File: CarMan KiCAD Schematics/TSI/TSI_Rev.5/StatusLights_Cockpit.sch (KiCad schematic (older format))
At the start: 18 parts, among them Q3 ZVP1320F, U1 RDE03110S12, U11 TLP293, U13 TLP293

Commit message: Organizational
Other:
- moved on the sheet: D11, Q3, R110, R15, R74, U11
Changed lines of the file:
@@
 $Descr A4 11693 8268
 encoding utf-8
-Sheet 6 6
+Sheet 5 6
 Title ""
 Date ""
@@
 L TSI_Rev.5-rescue:TLP293-CarMan_KiCAD_Library-TSI_Rev.5-rescue U11
 U 1 1 5F9A966C
-P 5900 1650
-F 0 "U11" H 5900 1850 50  0000 C CNN
-F 1 "TLP293" H 5900 1450 50  0000 C CNN
-F 2 "Package_SO:SOIC-4_4.55x2.6mm_P1.27mm" H 5700 1450 50  0001 L CIN
-F 3 "" H 5900 1650 50  0001 L CNN
-	1    5900 1650
+P 10125 3450
+F 0 "U11" H 10125 3650 50  0000 C CNN
+F 1 "TLP293" H 10125 3250 50  0000 C CNN
+F 2 "Package_SO:SOIC-4_4.55x2.6mm_P1.27mm" H 9925 3250 50  0001 L CIN
+F 3 "" H 10125 3450 50  0001 L CNN
+	1    10125 3450
 	1    0    0    -1
 $EndComp
@@
 L Device:R R15
 U 1 1 5F9DEF51
-P 5250 1550
-F 0 "R15" V 5150 1550 50  0000 C CNN
-F 1 "300" V 5250 1550 50  0000 C CNN
-F 2 "Resistor_SMD:R_0805_2012Metric_Pad1.15x1.40mm_HandSolder" V 5180 1550 50  0001 C CNN
-F 3 "~" H 5250 1550 50  0001 C CNN
-	1    5250 1550
+P 9475 3350
+F 0 "R15" V 9375 3350 50  0000 C CNN
+F 1 "300" V 9475 3350 50  0000 C CNN
+F 2 "Resistor_SMD:R_0805_2012Metric_Pad1.15x1.40mm_HandSolder" V 9405 3350 50  0001 C CNN
+F 3 "~" H 9475 3350 50  0001 C CNN
+	1    9475 3350
 	0    1    1    0
 $EndComp
-Text Label 6750 1550 2    50   ~ 0
+Text Label 10975 3350 2    50   ~ 0
 24V
-Text Label 6750 1750 2    50   ~ 0
+Text Label 10975 3550 2    50   ~ 0
 Drive_LED
-Text Label 4400 1750 0    50   ~ 0
-GLV_RTN
-Text Label 4400 1550 0    50   ~ 0
+Text Label 8625 3550 0    50   ~ 0
+GLV_RTN
+Text Label 8625 3350 0    50   ~ 0
 D_LED_CTRL
-Text Label 4700 3200 2    50   ~ 0
+Text Label 4525 3200 2    50   ~ 0
 24V
 Text HLabel 800  5850 0    50   Input ~ 0
@@
 Drive_BTN
 Wire Wire Line
-	5600 1550 5400 1550
+	9825 3350 9625 3350
 Text Notes 7100 6950 0    177  ~ 0
 STATUS LIGHTS, TSAL & RTDS
@@
 	0    1    1    0
 $EndComp
-Connection ~ 4450 3200
-Wire Wire Line
-	4450 3200 5100 3200
-Wire Wire Line
-	3900 3200 4450 3200
+Connection ~ 4275 3200
+Wire Wire Line
+	4275 3200 4925 3200
+Wire Wire Line
+	3725 3200 4275 3200
 $Comp
 L CarMan_KiCAD_Library:D_Schottky D11
 U 1 1 5F9B6857
-P 4450 3600
-F 0 "D11" V 4300 3700 50  0000 C CNN
-F 1 "MMSZ5231B-7-F" H 4450 3726 50  0001 C CNN
-F 2 "Diode_SMD:D_SOD-123" H 4450 3600 50  0001 C CNN
-F 3 "~" H 4450 3600 50  0001 C CNN
-	1    4450 3600
+P 4275 3600
+F 0 "D11" V 4125 3700 50  0000 C CNN
+F 1 "MMSZ5231B-7-F" H 4275 3726 50  0001 C CNN
+F 2 "Diode_SMD:D_SOD-123" H 4275 3600 50  0001 C CNN
+F 3 "~" H 4275 3600 50  0001 C CNN
+	1    4275 3600
 	0    1    1    0
 $EndComp
 Wire Wire Line
-	5100 4725 6150 4725
-Wire Wire Line
-	4450 3900 4800 3900
+	4925 4725 5975 4725
+Wire Wire Line
+	4275 3900 4625 3900
 $Comp
 L Device:Q_PMOS_GSD Q?
 U 1 1 5FC93215
-P 5000 3900
+P 4825 3900
 AR Path="/6196BF15/5FC93215" Ref="Q?"  Part="1"
 AR Path="/5FE1DCBA/5FC93215" Ref="Q3"  Part="1"
-F 0 "Q3" H 5204 3854 50  0000 L CNN
-F 1 "ZVP1320F" H 5204 3945 50  0000 L CNN
-F 2 "TSI_Rev_2021_Footprint_Lib:SOT23" H 5200 4000 50  0001 C CNN
-F 3 "https://www.snapeda.com/parts/ZVP1320FTA/Diodes%20Inc./datasheet/" H 5000 3900 50  0001 C CNN
-	1    5000 3900
+F 0 "Q3" H 5029 3854 50  0000 L CNN
+F 1 "ZVP1320F" H 5029 3945 50  0000 L CNN
+F 2 "TSI_Rev_2021_Footprint_Lib:SOT23" H 5025 4000 50  0001 C CNN
+F 3 "https://www.snapeda.com/parts/ZVP1320FTA/Diodes%20Inc./datasheet/" H 4825 3900 50  0001 C CNN
+	1    4825 3900
 	1    0    0    1
 $EndComp
 Wire Wire Line
-	3050 4100 2850 4100
-Wire Wire Line
 	2250 3900 2050 3900
-Text Notes 5200 4550 0    50   ~ 0
+Text Notes 5025 4550 0    50   ~ 0
 STA20502 RTDS BUZZER (.6A MAX)\n3/1/21 - Pulsed at max of 90mA\n3/1/21 - Tested RTDS, w/Xsistor, worked\n
 Wire Notes Line
-	5100 4575 5100 4625
-Wire Notes Line
-	5050 4375 5150 4375
-Wire Notes Line
-	5050 4575 5050 4375
-Wire Notes Line
-	5150 4575 5050 4575
-Wire Notes Line
-	5150 4375 5150 4575
-Wire Notes Line
-	5100 4325 5100 4375
-Text Label 5550 4725 2    50   ~ 0
-GLV_RTN
-Text Label 6150 4725 2    50   ~ 0
+	4925 4575 4925 4625
+Wire Notes Line
+	4875 4375 4975 4375
+Wire Notes Line
+	4875 4575 4875 4375
+Wire Notes Line
+	4975 4575 4875 4575
+Wire Notes Line
+	4975 4375 4975 4575
+Wire Notes Line
+	4925 4325 4925 4375
+Text Label 5375 4725 2    50   ~ 0
+GLV_RTN
+Text Label 5975 4725 2    50   ~ 0
 RTDS_RTN
-Text Label 5350 4250 0    50   ~ 0
+Text Label 5250 4250 2    50   ~ 0
 RTDS
 Wire Wire Line
-	5100 4250 5350 4250
-Wire Wire Line
-	5100 4100 5100 4250
-Connection ~ 4450 3900
-Wire Wire Line
-	5100 3200 5100 3700
-Text Label 3050 4100 0    50   ~ 0
+	4925 4100 4925 4250
+Connection ~ 4275 3900
+Wire Wire Line
+	4925 3200 4925 3700
+Text Label 3700 4100 2    50   ~ 0
 GLV_RTN
 $Comp
@@
 $EndComp
 Wire Wire Line
-	4450 3450 4450 3200
-Wire Wire Line
-	3900 3450 3900 3200
-Connection ~ 3900 3900
-Wire Wire Line
-	4450 3900 4450 3750
-Wire Wire Line
-	3900 3900 4450 3900
-Wire Wire Line
-	3900 3900 3900 3750
-Wire Wire Line
-	3550 3900 3900 3900
-Wire Wire Line
-	2850 3900 3250 3900
+	4275 3450 4275 3200
+Wire Wire Line
+	3725 3450 3725 3200
+Connection ~ 3725 3900
+Wire Wire Line
+	4275 3900 4275 3750
+Wire Wire Line
+	3725 3900 4275 3900
+Wire Wire Line
+	3725 3900 3725 3750
+Wire Wire Line
+	3375 3900 3725 3900
 $Comp
 L Device:R R74
 U 1 1 5F9BC6E2
-P 3900 3600
-F 0 "R74" H 3970 3646 50  0000 L CNN
-F 1 "40K" V 3900 3550 50  0000 L CNN
-F 2 "Resistor_SMD:R_0805_2012Metric_Pad1.15x1.40mm_HandSolder" V 3830 3600 50  0001 C CNN
-F 3 "~" H 3900 3600 50  0001 C CNN
-	1    3900 3600
+P 3725 3600
+F 0 "R74" H 3795 3646 50  0000 L CNN
+F 1 "40K" V 3725 3550 50  0000 L CNN
+F 2 "Resistor_SMD:R_0805_2012Metric_Pad1.15x1.40mm_HandSolder" V 3655 3600 50  0001 C CNN
+F 3 "~" H 3725 3600 50  0001 C CNN
+	1    3725 3600
 	1    0    0    -1
 $EndComp
@@
 L Device:R R110
 U 1 1 5F9BBE04
-P 3400 3900
-F 0 "R110" V 3300 3900 50  0000 C CNN
-F 1 "10K" V 3400 3900 50  0000 C CNN
-F 2 "Resistor_SMD:R_0805_2012Metric_Pad1.15x1.40mm_HandSolder" V 3330 3900 50  0001 C CNN
-F 3 "~" H 3400 3900 50  0001 C CNN
-	1    3400 3900
+P 3225 3900
+F 0 "R110" V 3125 3900 50  0000 C CNN
+F 1 "10K" V 3225 3900 50  0000 C CNN
+F 2 "Resistor_SMD:R_0805_2012Metric_Pad1.15x1.40mm_HandSolder" V 3155 3900 50  0001 C CNN
+F 3 "~" H 3225 3900 50  0001 C CNN
+	1    3225 3900
 	0    1    1    0
 $EndComp
@@
 	4400 7000 5000 7000
 Wire Wire Line
-	4400 1550 5100 1550
-Wire Wire Line
-	4400 1750 5600 1750
-Wire Wire Line
-	6200 1550 6750 1550
-Wire Wire Line
-	6200 1750 6750 1750
+	8625 3350 9325 3350
+Wire Wire Line
+	8625 3550 9825 3550
+Wire Wire Line
+	10425 3350 10975 3350
+Wire Wire Line
+	10425 3550 10975 3550
 Wire Notes Line
 	500  2100 2250 2100
@@
 GLV_RTN
 Wire Wire Line
-	5100 4250 5100 4325
-Connection ~ 5100 4250
-Wire Wire Line
-	5100 4625 5100 4725
+	4925 4250 4925 4325
+Connection ~ 4925 4250
+Wire Wire Line
+	4925 4625 4925 4725
+Wire Wire Line
+	4925 4250 5250 4250
+Wire Wire Line
+	2850 3900 3075 3900
+Wire Wire Line
+	2850 4100 3700 4100
 $EndSCHEMATC

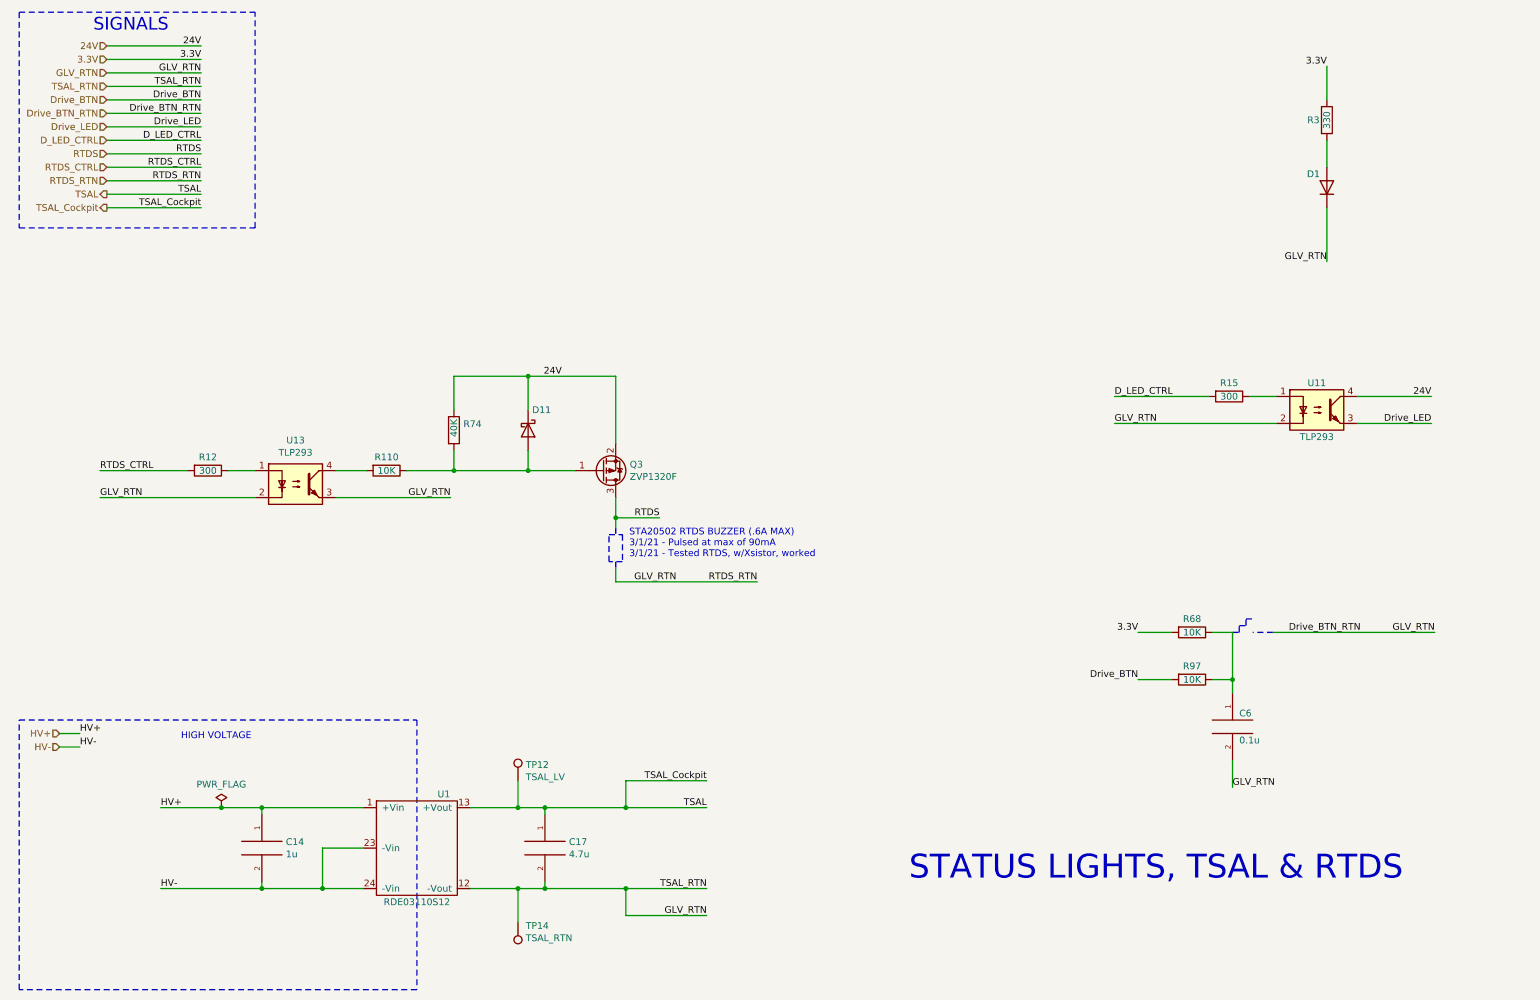
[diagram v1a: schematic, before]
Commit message: TSI Updated & error fixes: added pull down resistors, and 5V_ISO_RTN
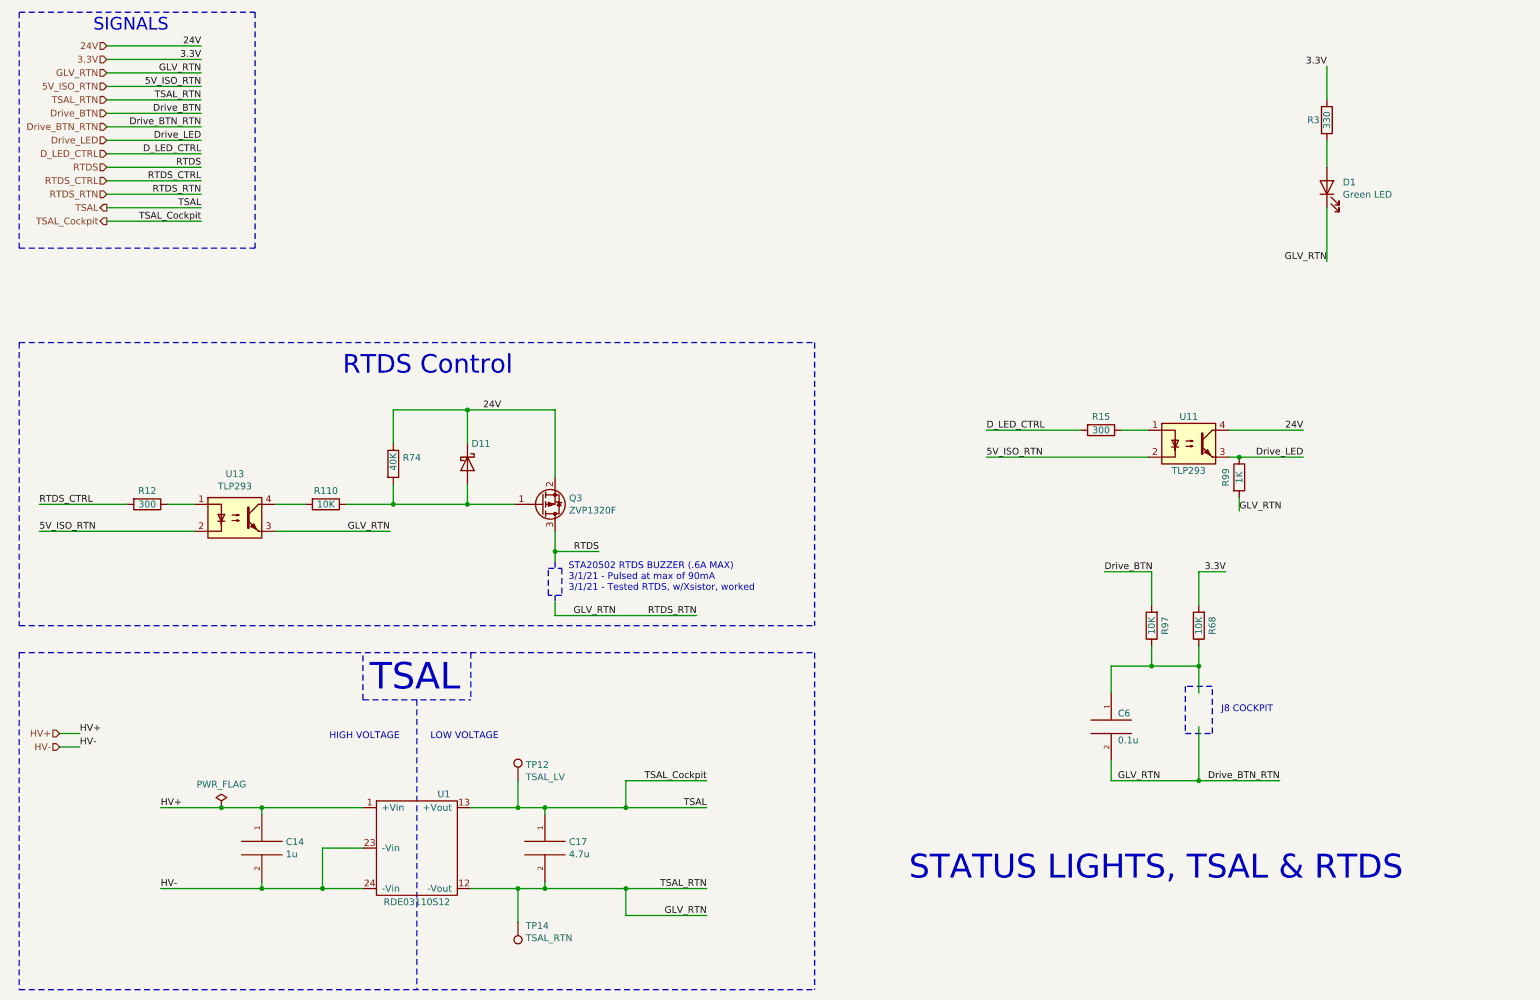
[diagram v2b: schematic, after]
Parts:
- removed D1: Green LED, LED_SMD:LED_0805_2012Metric_Pad1.15x1.40mm_HandSolder, symbol Device:D
- added D1: Green LED, LED_SMD:LED_0805_2012Metric_Pad1.15x1.40mm_HandSolder, symbol Device:LED
- added R99: 1K, Resistor_SMD:R_0805_2012Metric_Pad1.15x1.40mm_HandSolder, symbol Device:R
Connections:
- net labels added: 5V_ISO_RTN
- wire segments 77 -> 86
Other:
- note added: "J8 COCKPIT\n"
- note added: "LOW VOLTAGE\n"
- note added: "RTDS Control"
- note added: "TSAL"
- moved on the sheet: C6, D11, Q3, R110, R12, R15, R68, R74, R97, U11, U13

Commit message: Updated C14 with mouser part number
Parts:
- C14: Mouser Part# (none) -> B32522C3105J189
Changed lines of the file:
@@
 F 2 "Capacitor_THT:C_Rect_L18.0mm_W9.0mm_P15.00mm_FKS3_FKP3" H 2300 6700 50  0001 C CNN
 F 3 "https://www.tdk-electronics.tdk.com/inf/20/20/db/fc_2009/B32520_529.pdf" H 2300 6700 50  0001 C CNN
+F 4 "B32522C3105J189" H 2300 6700 50  0001 C CNN "Mouser Part#"
 	1    2300 6700
 	1    0    0    -1

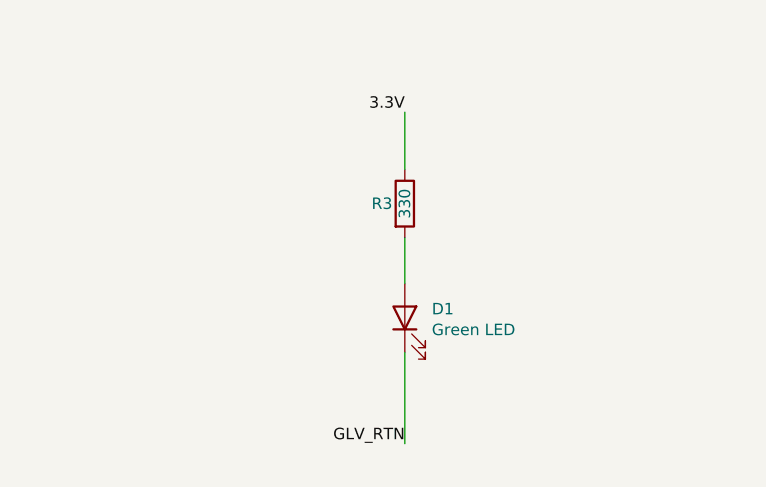
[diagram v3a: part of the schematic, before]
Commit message: - removed testing headers (All pins were easily testable, one that weren't received testing points) - Added pull up resistor at drain of SCADA Relay - Fixed issue with U27-PC_Ready signal not being isolated, also added pull down resistor. Comment about 5V_ISO from logic is necessary - Increased Resistor values across D1 and D4 to cut intensity - Updated PCB board with Netlist
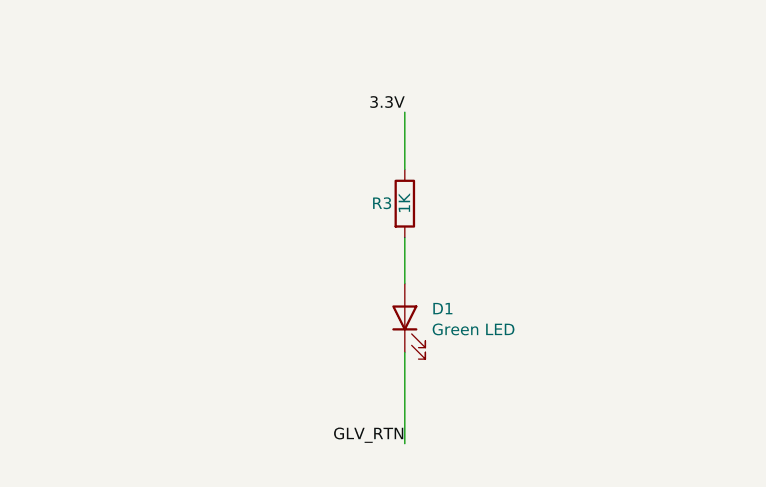
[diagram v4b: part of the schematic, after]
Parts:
- R3: value 330 -> 1K
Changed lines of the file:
@@
 P 10200 1300
 F 0 "R3" H 10100 1300 50  0000 C CNN
-F 1 "330" V 10200 1300 50  0000 C CNN
+F 1 "1K" V 10200 1300 50  0000 C CNN
 F 2 "Resistor_SMD:R_0805_2012Metric_Pad1.15x1.40mm_HandSolder" V 10130 1300 50  0001 C CNN
 F 3 "~" H 10200 1300 50  0001 C CNN
